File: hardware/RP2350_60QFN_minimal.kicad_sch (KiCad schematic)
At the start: 37 parts, among them J4 SM03B-SRSS-TB, J5 4677, SW1 SW_Push, SW2 SW_Push, U1 RP2350_60QFN, U3 W25Q128JVS, Y1 ABM8-272-T3

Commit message: Trig finished
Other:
- sheet Trigger ports: added ASIG, ASIG2, SCL, SDA, TRIG, TRIG2, VREF, VSYS; removed none
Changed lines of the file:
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@@
+			)
+		)
+		(pin "ASIG" input
+			(at 189.23 45.72 180)
+			(effects
+				(font
+					(size 1.27 1.27)
+				)
+				(justify left)
+			)
+		)
+		(pin "ASIG2" input
+			(at 189.23 48.26 180)
+			(effects
+				(font
+					(size 1.27 1.27)
+				)
+				(justify left)
+			)
+		)
+		(pin "SCL" input
+			(at 189.23 50.8 180)
+			(effects
+				(font
+					(size 1.27 1.27)
+				)
+				(justify left)
+			)
+		)
+		(pin "SDA" input
+			(at 189.23 53.34 180)
+			(effects
+				(font
+					(size 1.27 1.27)
+				)
+				(justify left)
+			)
+		)
+		(pin "TRIG" output
+			(at 217.17 52.07 0)
+			(effects
+				(font
+					(size 1.27 1.27)
+				)
+				(justify right)
+			)
+		)
+		(pin "VREF" input
+			(at 189.23 55.88 180)
+			(effects
+				(font
+					(size 1.27 1.27)
+				)
+				(justify left)
+			)
+		)
+		(pin "VSYS" input
+			(at 189.23 58.42 180)
+			(effects
+				(font
+					(size 1.27 1.27)
+				)
+				(justify left)
+			)
+		)
+		(pin "TRIG2" output
+			(at 217.17 54.61 0)
+			(effects
+				(font
+					(size 1.27 1.27)
+				)
+				(justify right)
 			)
 		)

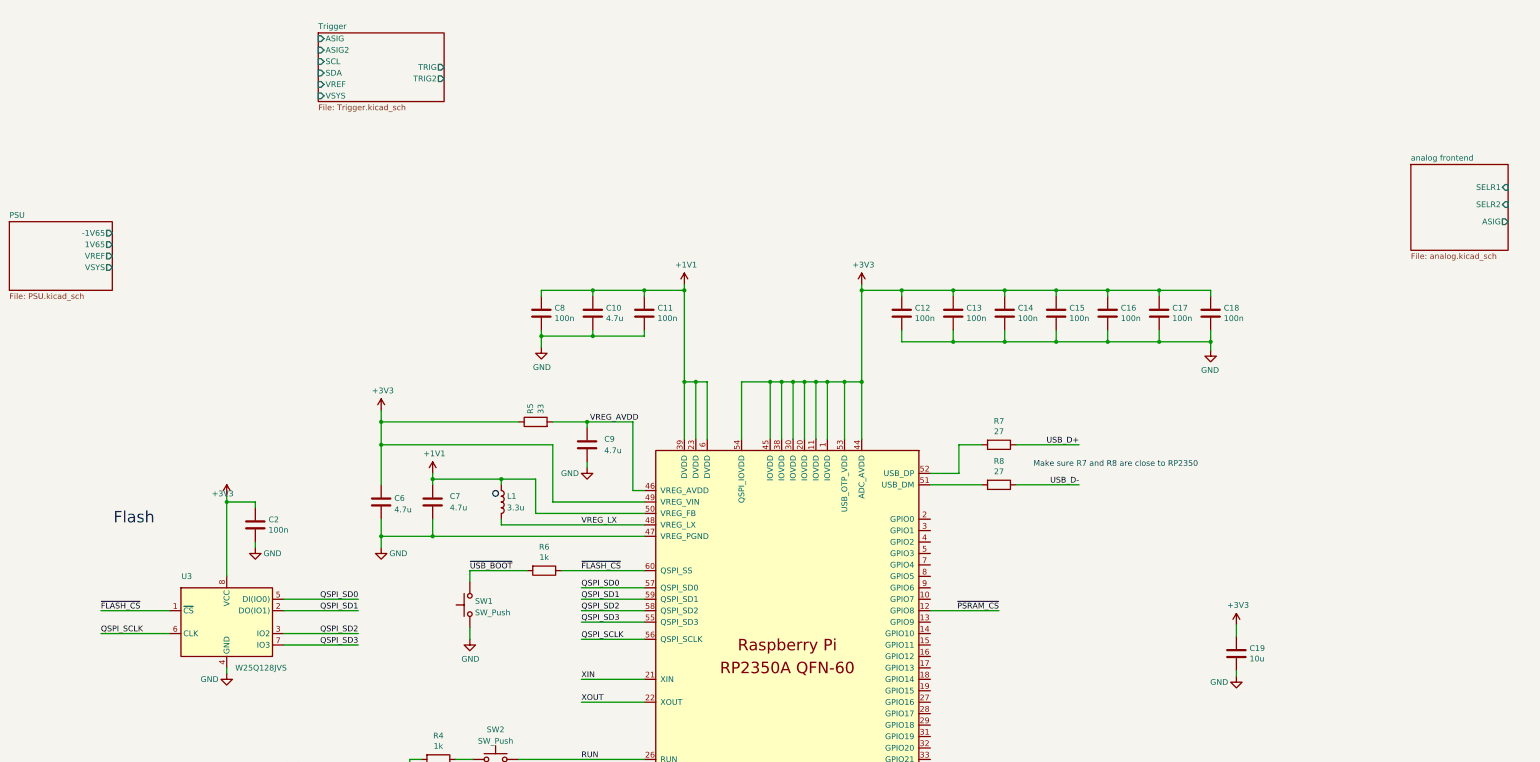
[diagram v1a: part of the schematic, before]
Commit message: connected analog i/o on main schematic and updated PSU naming
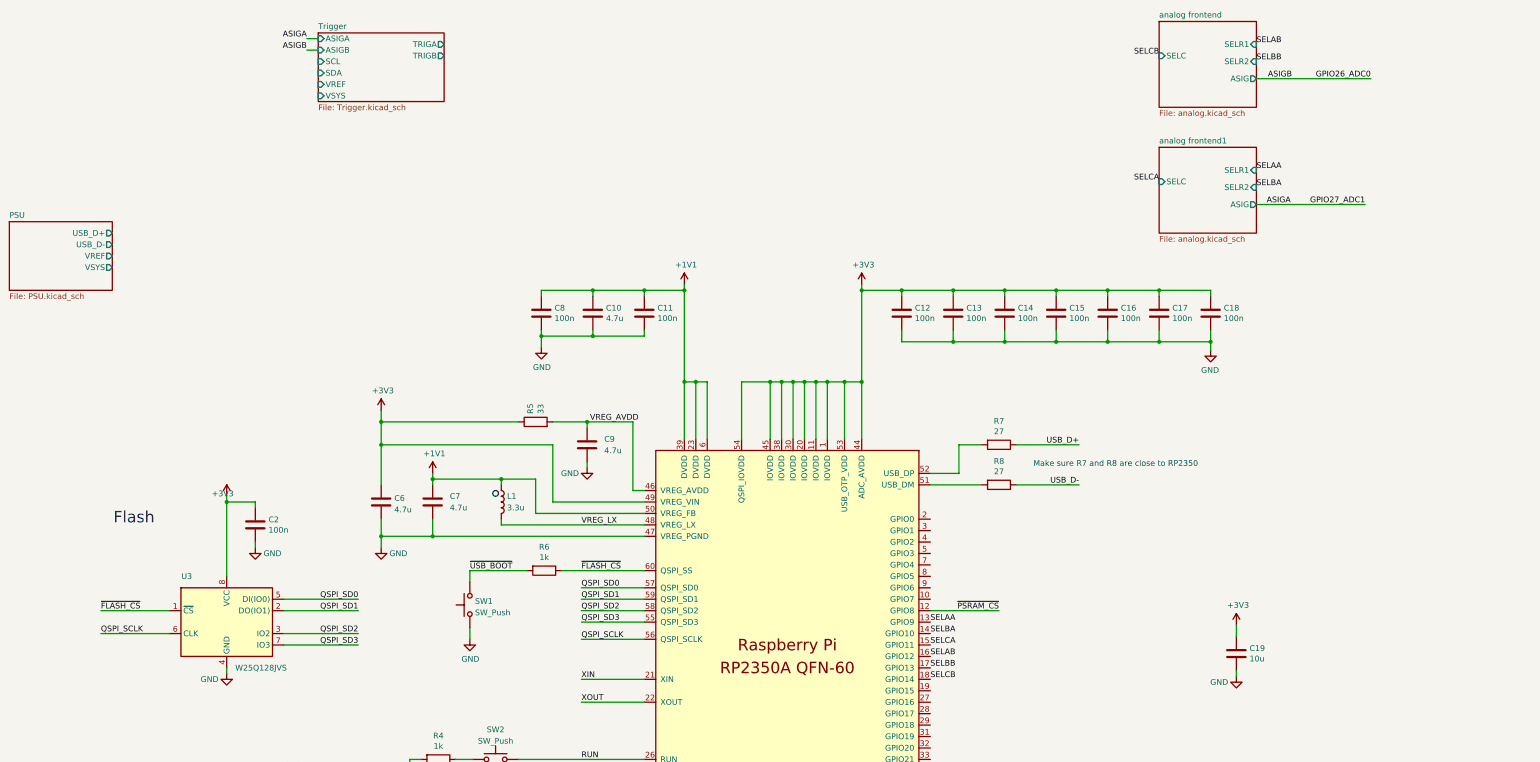
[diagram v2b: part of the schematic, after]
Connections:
- net SELAA: now reaches U1.13 (GPIO9)
- net SELBA: now reaches U1.14 (GPIO10)
- net SELCA: now reaches U1.15 (GPIO11)
- net SELAB: now reaches U1.16 (GPIO12)
- net SELBB: now reaches U1.17 (GPIO13)
- net SELCB: now reaches U1.18 (GPIO14)
- net GPIO26_ADC0 renamed ASIGB
- net GPIO27_ADC1 renamed ASIGA
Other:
- added sheet analog frontend1 (analog.kicad_sch)
- sheet PSU ports: added USB_D+, USB_D-; removed -1V65, 1V65
- sheet Trigger ports: added ASIGA, ASIGB, TRIGA, TRIGB; removed ASIG, ASIG2, TRIG, TRIG2
- sheet analog frontend ports: added SELC; removed none

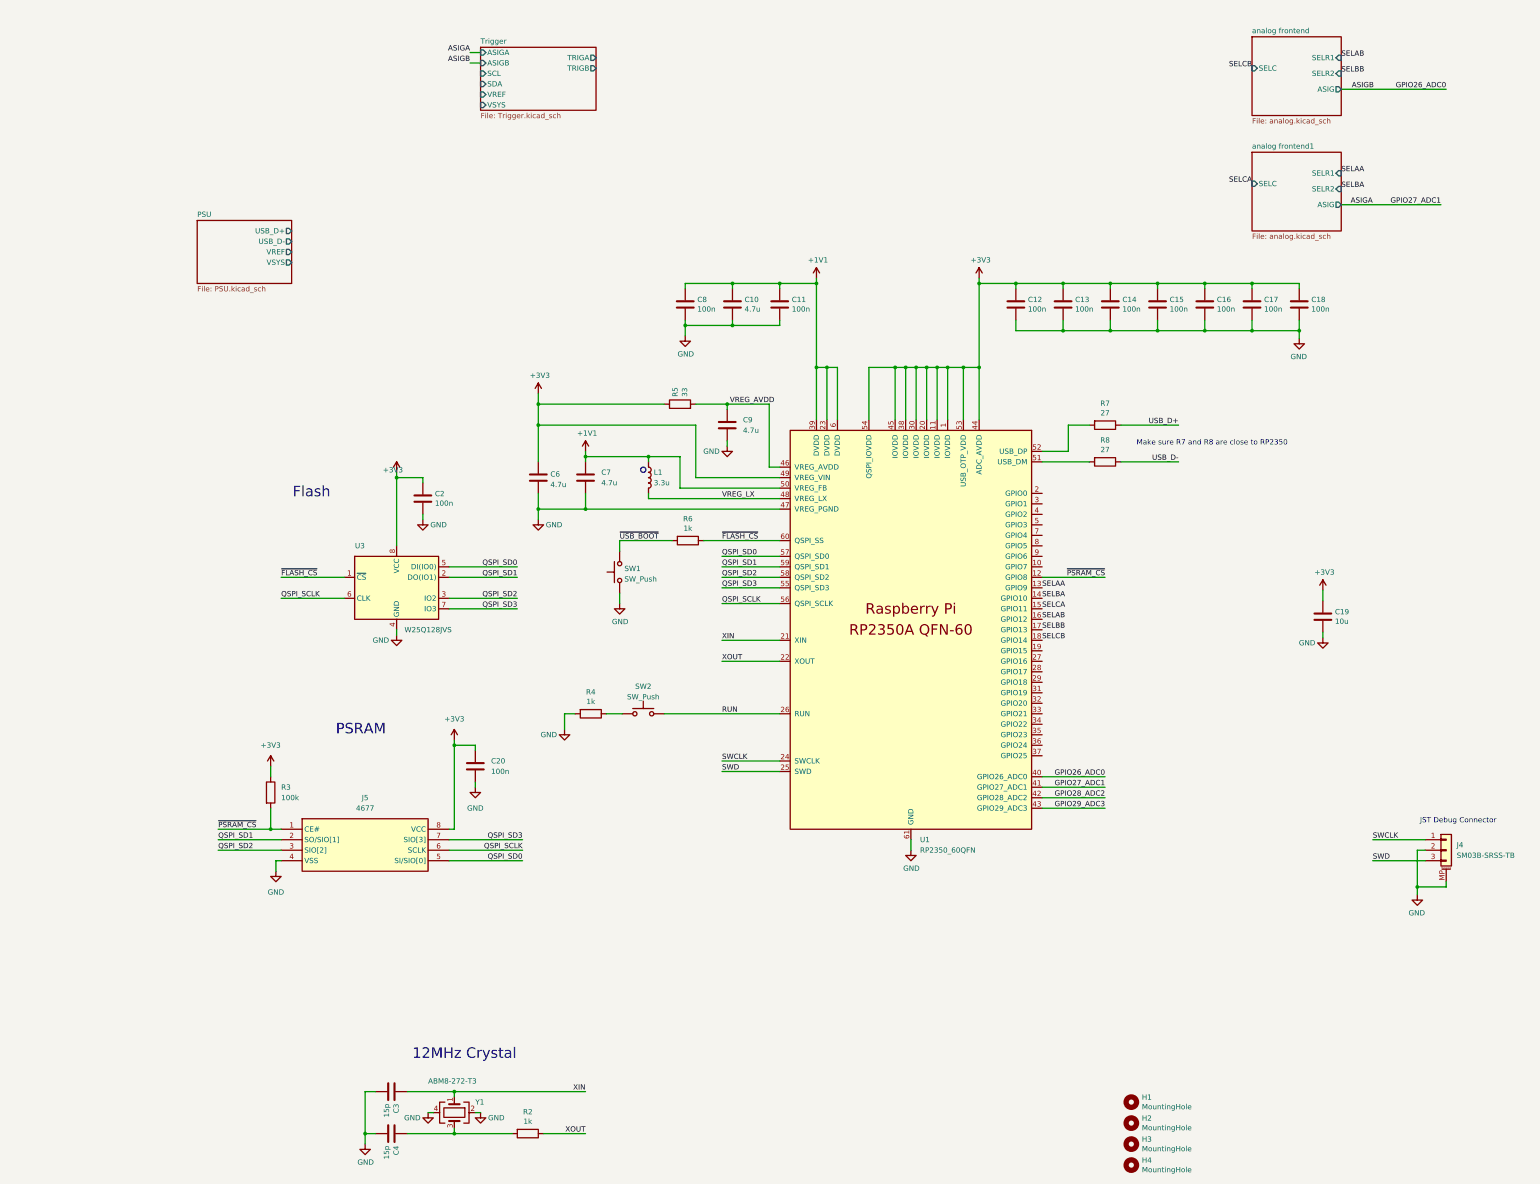
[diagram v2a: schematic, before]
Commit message: feat(hardware): Cleanup schematic, replace offset stage with non-inverting op amp, add neopixel LED
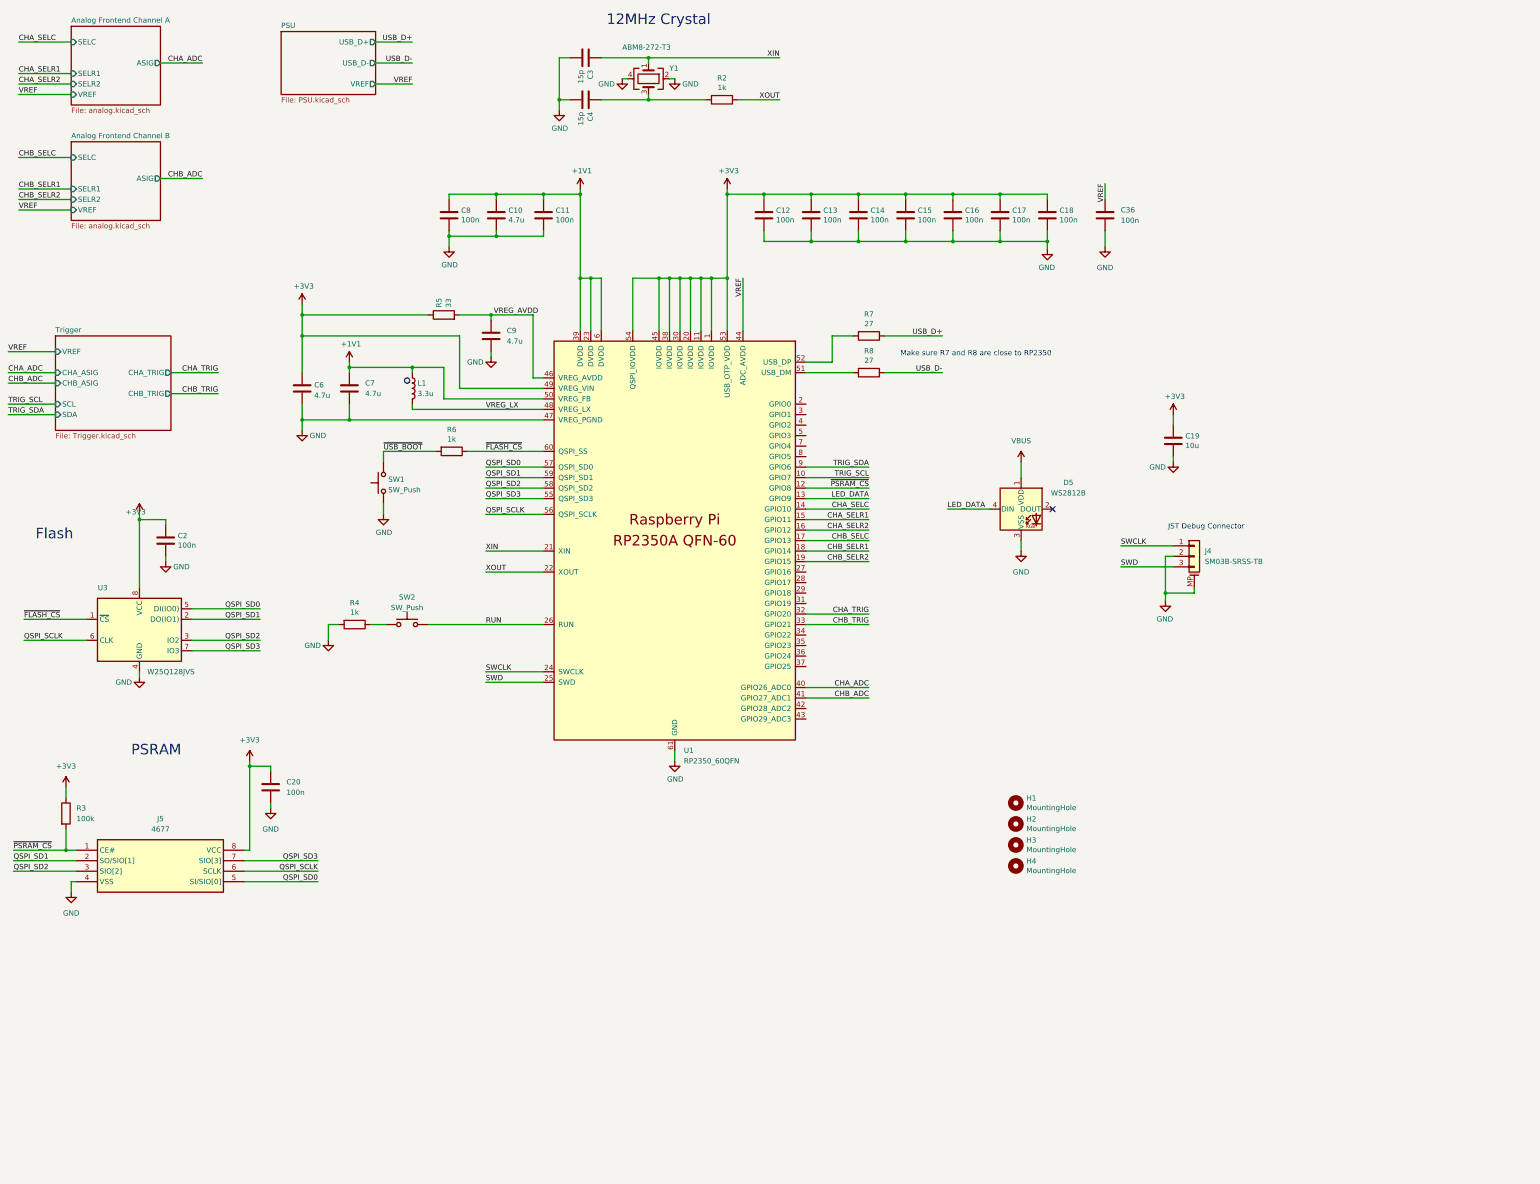
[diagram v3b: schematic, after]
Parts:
- added C36: 100n, symbol Device:C
- added D5: WS2812B, LED_SMD:LED_WS2812B_PLCC4_5.0x5.0mm_P3.2mm, symbol LED:WS2812B
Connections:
- net +3V3: no longer U1.44 (ADC_AVDD)
- net GND: now also C36.2, D5.3 (VSS)
- net TRIG_SCL: now reaches U1.10 (GPIO7)
- net CHB_SELR2: now reaches U1.19 (GPIO15)
- net CHA_TRIG: now reaches U1.32 (GPIO20)
- net CHB_TRIG: now reaches U1.33 (GPIO21)
- net TRIG_SDA: now reaches U1.9 (GPIO6)
- net ASIGA renamed CHB_ADC
- net ASIGB renamed CHA_ADC
- net GPIO28_ADC2: no longer names the net of U1.42 (GPIO28_ADC2)
- net GPIO29_ADC3: no longer names the net of U1.43 (GPIO29_ADC3)
- net SELAA renamed LED_DATA
- net LED_DATA: now also D5.4 (DIN)
- net SELAB renamed CHA_SELR2
- net SELBA renamed CHA_SELC
- net SELBB renamed CHB_SELC
- net SELCA renamed CHA_SELR1
- net SELCB renamed CHB_SELR1
- new net VBUS: D5.1 (VDD)
- new net VREF: C36.1, U1.44 (ADC_AVDD)
- no-connect marks 0 -> 1
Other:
- sheet analog frontend renamed Analog Frontend Channel A
- sheet analog frontend1 renamed Analog Frontend Channel B
- sheet Analog Frontend Channel A ports: added VREF; removed none
- sheet Analog Frontend Channel B ports: added VREF; removed none
- sheet PSU ports: added none; removed VSYS
- sheet Trigger ports: added CHA_ASIG, CHA_TRIG, CHB_ASIG, CHB_TRIG; removed ASIGA, ASIGB, TRIGA, TRIGB, VSYS
- moved on the sheet: C10, C11, C12, C13, C14, C15, C16, C17, C18, C19, C2, C20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

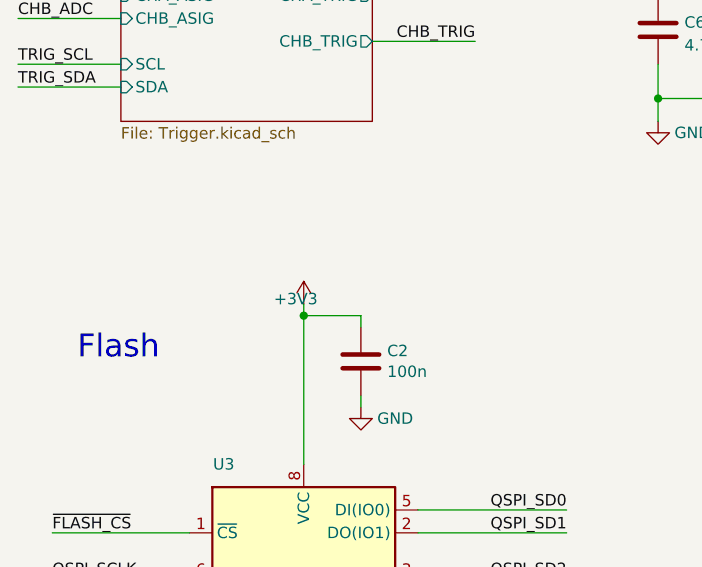
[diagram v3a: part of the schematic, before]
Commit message: fix(hardware): Make power rail net naming consistent
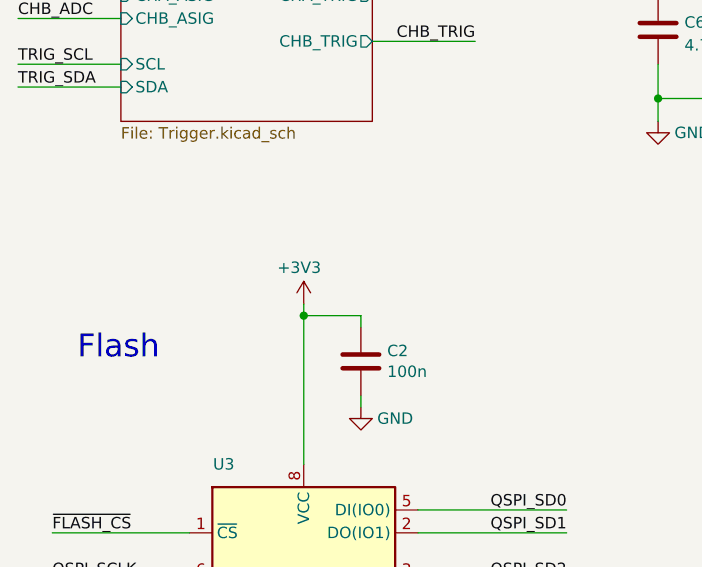
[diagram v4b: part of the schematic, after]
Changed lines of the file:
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@@
 		)
 		(property "Value" "+3V3"
-			(at 105.791 156.8958 0)
+			(at 106.172 153.416 0)
 			(effects
 				(font

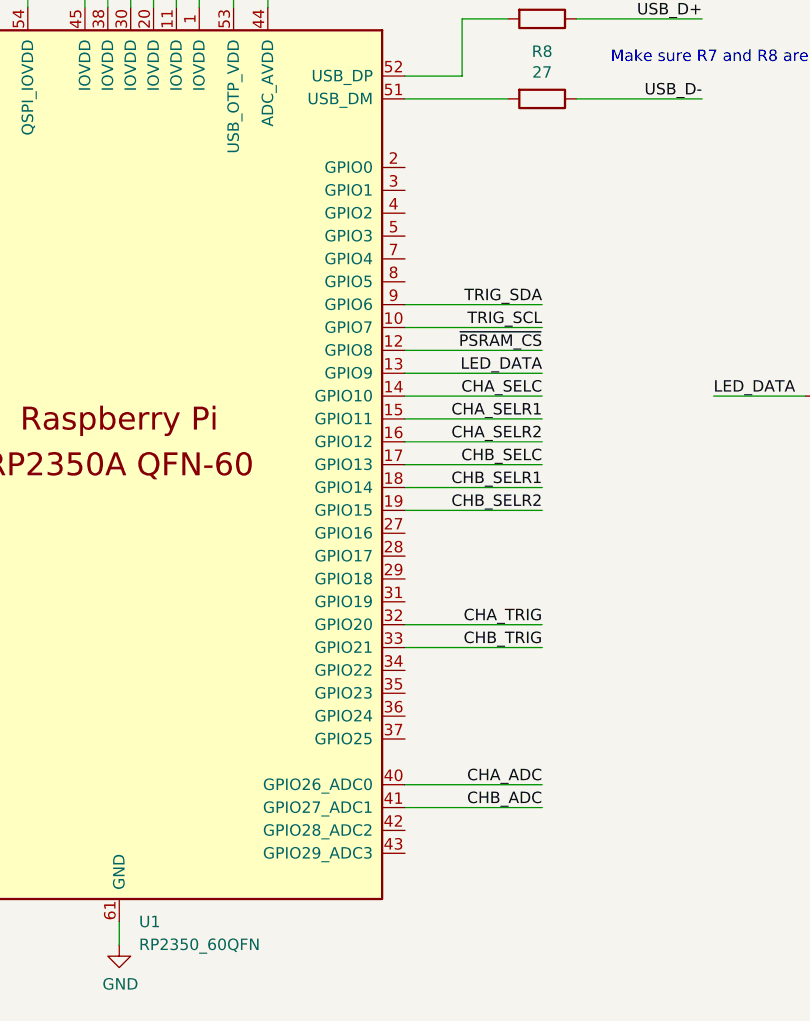
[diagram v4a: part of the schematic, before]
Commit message: feat(hardware): Add zero ohm resistor before analog input
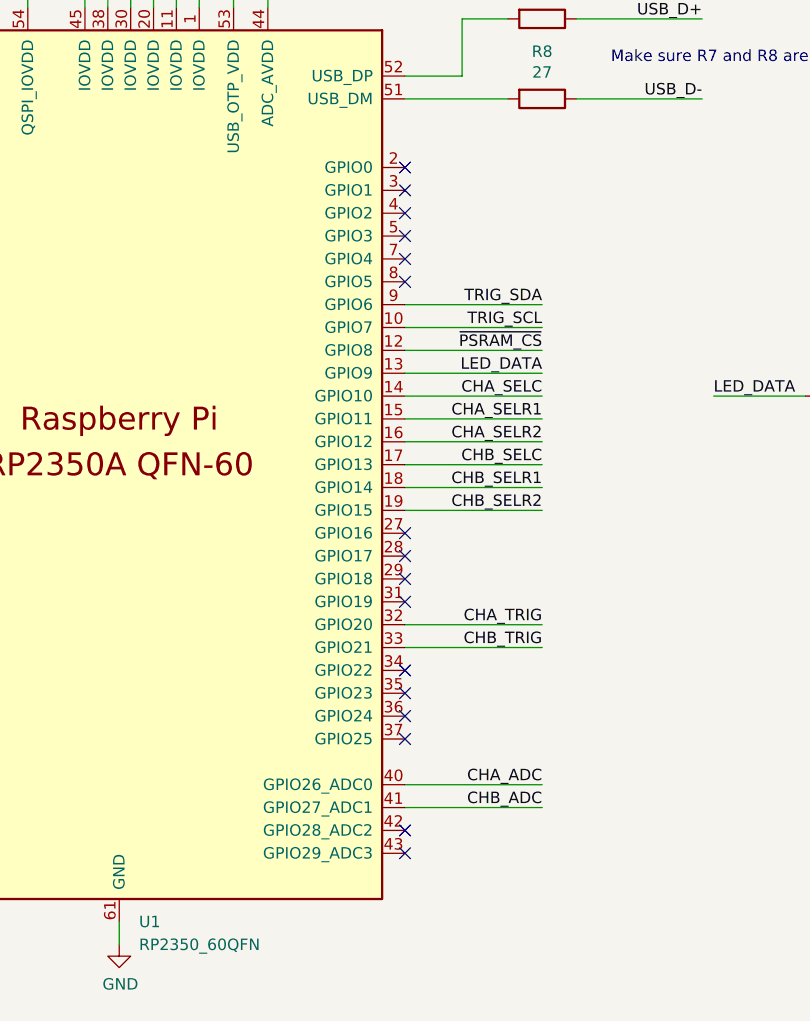
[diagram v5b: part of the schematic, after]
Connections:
- no-connect marks 1 -> 17
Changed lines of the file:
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@@
+	)
+	(no_connect
+		(at 267.97 171.45)
+	)
+	(no_connect
+		(at 267.97 135.89)
+	)
+	(no_connect
+		(at 267.97 133.35)
+	)
+	(no_connect
+		(at 267.97 138.43)
+	)
+	(no_connect
+		(at 267.97 189.23)
+	)
+	(no_connect
+		(at 267.97 186.69)
+	)
+	(no_connect
+		(at 267.97 207.01)
+	)
+	(no_connect
+		(at 267.97 194.31)
+	)
+	(no_connect
+		(at 267.97 204.47)
+	)
+	(no_connect
+		(at 267.97 140.97)
 	)
 	(no_connect
 		(at 327.66 156.21)
 	)
+	(no_connect
+		(at 267.97 191.77)
+	)
+	(no_connect
+		(at 267.97 130.81)
+	)
+	(no_connect
+		(at 267.97 179.07)
+	)
+	(no_connect
+		(at 267.97 173.99)
+	)
+	(no_connect
+		(at 267.97 176.53)
+	)
+	(no_connect
+		(at 267.97 143.51)
+	)
 	(wire

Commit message: added footprints
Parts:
- C20, C36: footprint (none) -> Capacitor_SMD:C_0402_1005Metric
- J5: footprint SOIC127P600X175-8N -> PSRAM_Adafruit_4677:SOIC127P600X175-8N
- R3: footprint (none) -> Resistor_SMD:R_0402_1005Metric
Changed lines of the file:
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@@
 			)
 		)
-		(property "Footprint" "SOIC127P600X175-8N"
+		(property "Footprint" "PSRAM_Adafruit_4677:SOIC127P600X175-8N"
 			(at 128.27 333.68 0)
 			(effects
@@
 			)
 		)
-		(property "Footprint" ""
+		(property "Footprint" "Resistor_SMD:R_0402_1005Metric"
 			(at 87.122 229.87 90)
 			(effects
@@
 			)
 		)
-		(property "Footprint" ""
+		(property "Footprint" "Capacitor_SMD:C_0402_1005Metric"
 			(at 341.3252 88.9 0)
 			(effects
@@
 			)
 		)
-		(property "Footprint" ""
+		(property "Footprint" "Capacitor_SMD:C_0402_1005Metric"
 			(at 139.3952 227.33 0)
 			(effects
